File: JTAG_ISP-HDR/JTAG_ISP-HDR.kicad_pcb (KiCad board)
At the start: 2 copper layers, 23.1 x 46.1 mm, 11 parts, among them J1 Conn_01x08, J2 Conn_01x08

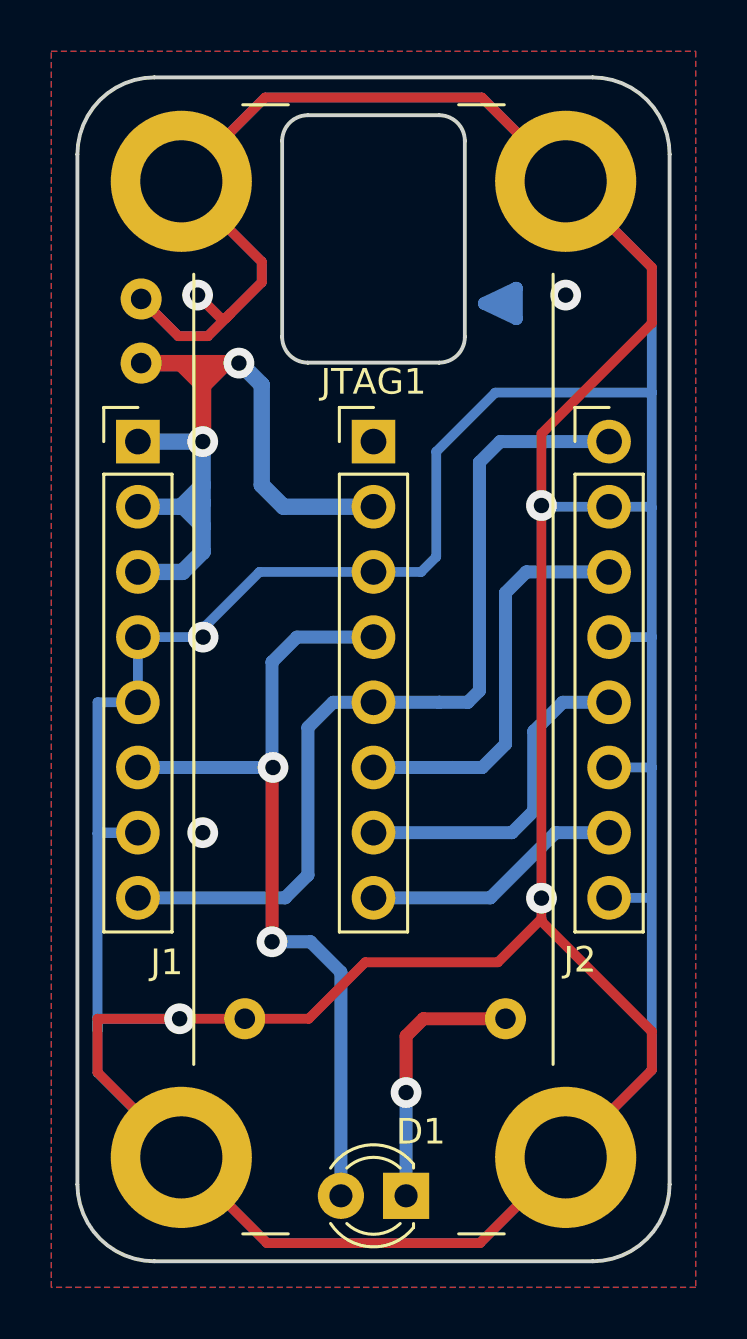
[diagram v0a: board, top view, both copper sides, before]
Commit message: # [PCB] + Ajout silkscreen autour du trou pour le connecteur ISP; * Alignement des silkscreen pour le nom des pièces; * Flèche indiquant la broche #1 est transférée sur le silkscreen; * Reroutage du ground; * Suppression de vias inutiles; * Mise à jour des fichiers gerbers; * Mise à jour de la cartouche;     * Date actuelle;     * Version actuelle.
# [SCHÉMA]
* Mise à jour de la cartouche;
    * Date actuelle;
    * Version actuelle.
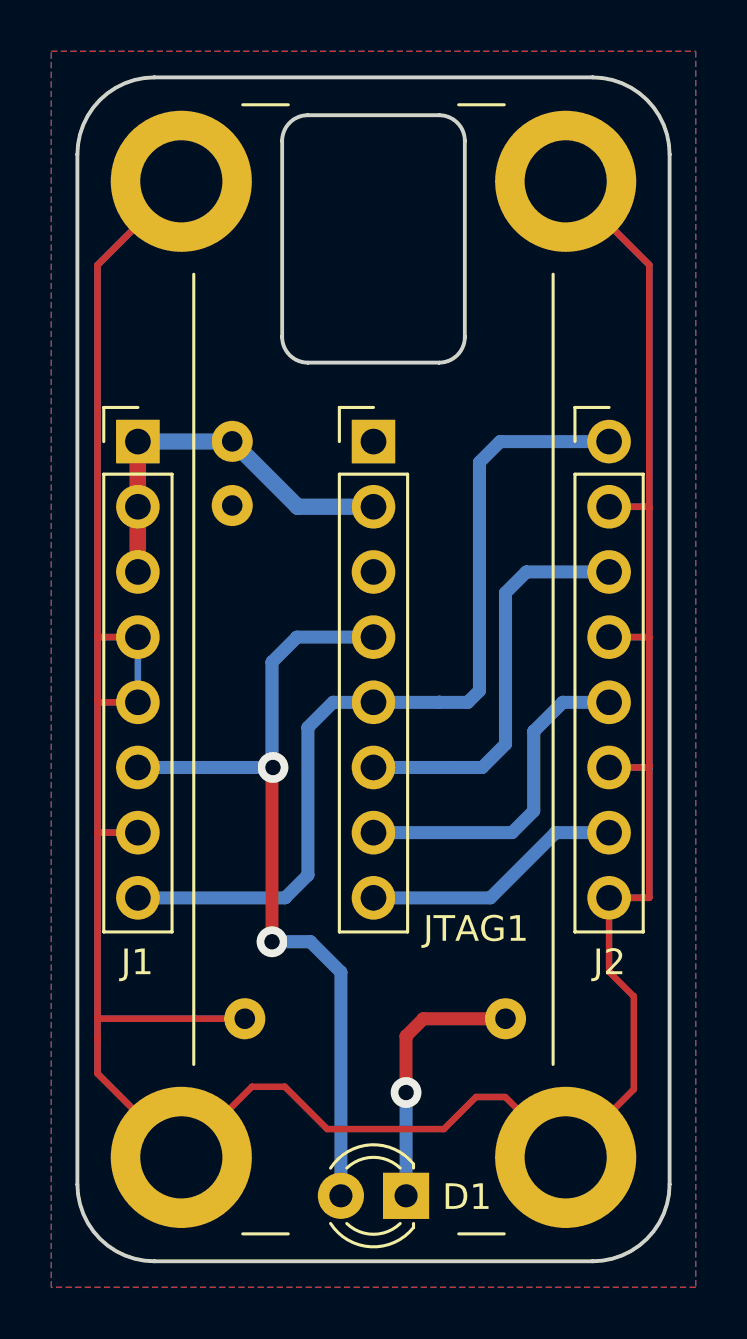
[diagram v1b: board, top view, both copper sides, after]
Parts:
- removed the REF** at (117.3, 57.4)
- added REF**: Fleche_small-silkscreen, THOMAS_library:Fleche_small-silkscreen, B.Cu at (117.3, 57.4)
- moved C1 4.68 mm to (106.2, 62.4), turned to -90 degrees
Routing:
- net GND: track 273.3 -> 206.2 mm, vias 7 -> 0
- net +5V: track 35.3 -> 20.4 mm, vias 2 -> 0
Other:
- board text added: "ISP"

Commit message: **# [PCB]** + Création d'une version avec des composants montés en surface à partir de la version précédente.
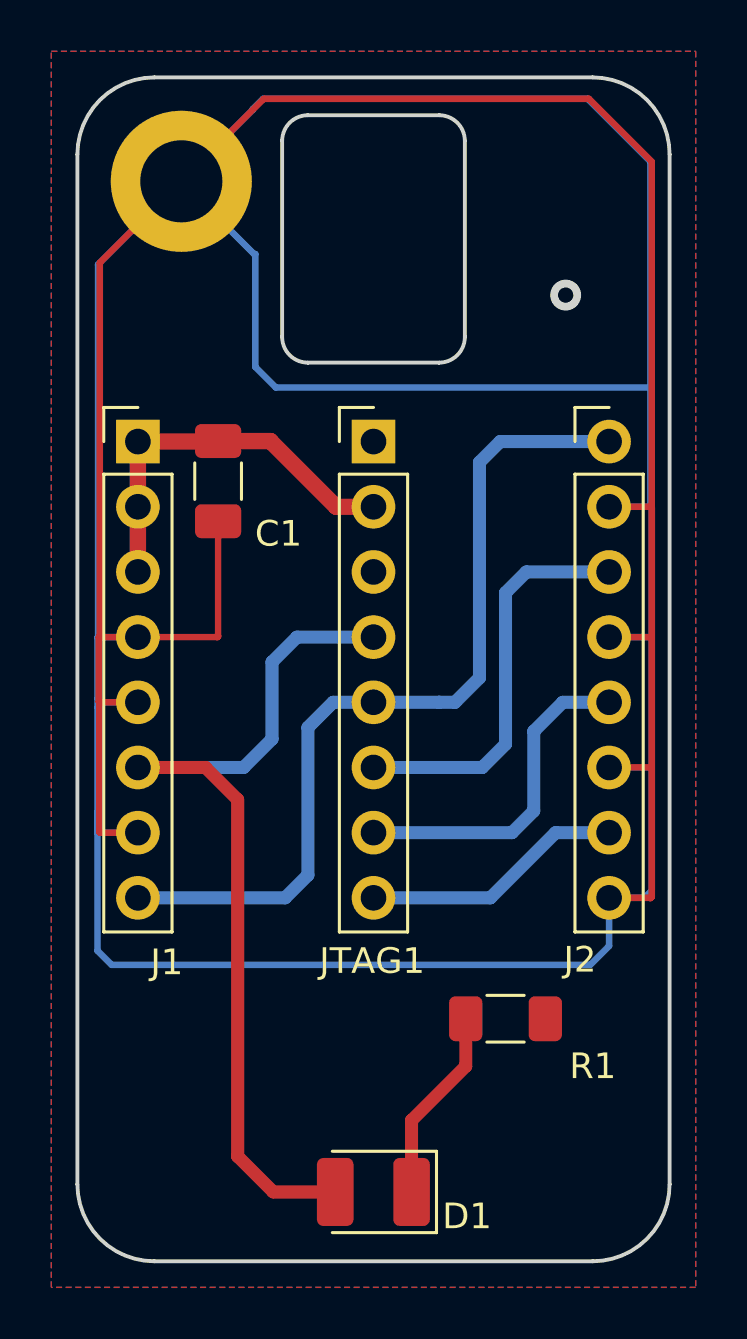
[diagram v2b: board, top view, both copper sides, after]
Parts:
- removed the REF** at (119.2, 90.3)
- removed the REF** at (104.2, 90.3)
- removed the REF** at (119.2, 52.3)
- C1: footprint Capacitor_THT:C_Disc_D3.0mm_W2.0mm_P2.50mm -> Capacitor_SMD:C_1206_3216Metric_Pad1.33x1.80mm_HandSolder; moved to F.Cu
- D1: footprint LED_THT:LED_D3.0mm -> LED_SMD:LED_1210_3225Metric_Pad1.42x2.65mm_HandSolder
- JTAG1: footprint THOMAS_library:PicKit4-2 -> Connector_PinHeader_2.54mm:PinHeader_1x08_P2.54mm_Vertical
- R1: footprint Resistor_THT:R_Axial_DIN0207_L6.3mm_D2.5mm_P10.16mm_Horizontal -> Resistor_SMD:R_1206_3216Metric_Pad1.30x1.75mm_HandSolder; moved to F.Cu
- moved C1 1.64 mm to (105.7, 63.9)
- moved D1 1.28 mm to (111.7, 91.6)
- turned R1 to 0 degrees
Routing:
- net GND: track 206.2 -> 233.9 mm, vias 0 -> 1
- net TDO: track 32.4 -> 35.7 mm, vias 2 -> 0
- net Net-(D1-Pad1): track 10.4 -> 7.63 mm, vias 1 -> 0
